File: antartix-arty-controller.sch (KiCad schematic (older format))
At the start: 113 parts, among them IC1 FT2232D, J1 QTE-020-04-L-D-A, J2 614004185023, J3 614004185023, J4 614004185023, J5 WE_629105150521, J6 0022232041, U1 PCT2075GVX, U2 PAC1934T-I_JQ, U3 USB2514B-I_M2, U4 TPS2024DR, U5 TPS2024DR, U6 TPS2024DR, Y1 7C-24.000MBB-T, Y2 MQ-6.000-12-30_30_

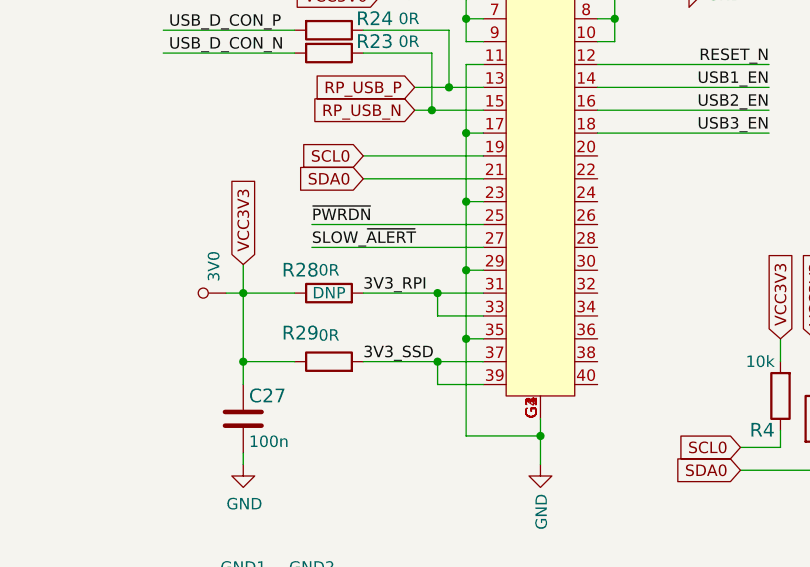
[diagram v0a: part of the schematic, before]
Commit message: Merge PCB design - Revision bumped to 1.1.0
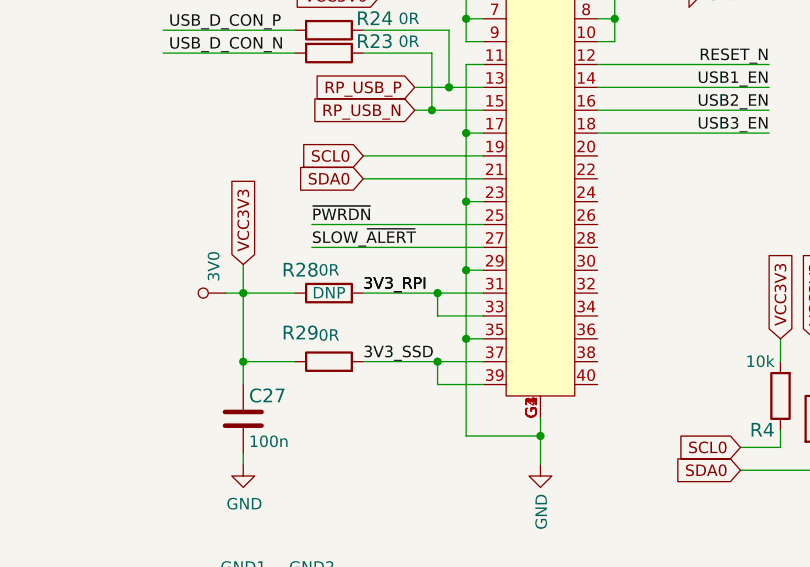
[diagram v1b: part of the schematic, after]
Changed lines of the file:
@@
 F1 "antartix-hdmi-adapter.sch" 50
 $EndSheet
+Text Label 1425 3225 0    50   ~ 0
+3V3_RPI
 $EndSCHEMATC

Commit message: Add hierarchical structure
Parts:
- removed 3V0, 5V0, GND1, GND2: TP_SMD1MM, antartix-arty-controller-footprints:Testpoint_smd_1mm, symbol antartix-arty-controller:TP_SMD1MM
- removed C1, C10, C11, C12, C13, C14, C15, C16, C17, C18, C2, C20, C22, C23, C24, C26, C27, C3, C32, C34, C35, C41, C42, C43, C44, C45, C46, C49, C5, C7, C9: C_100n_0402, antartix-arty-controller-footprints:0402-cap, symbol antartix-arty-controller:C_100n_0402
- removed C19, C21: C_22p_0402, antartix-arty-controller-footprints:0402-cap, symbol antartix-arty-controller:C_22p_0402
- removed C28, C29, C30: C_100n_0603, antmicro-footprints:0603-cap, symbol antmicroCapacitors0603:C_100n_0603
- removed C31, C33, C37, C47, C48: C_470u_KEMET_D, antartix-arty-controller-footprints:KEMET_D, symbol antartix-arty-controller:C_470u_KEMET_D
- removed C36, C38, C39: C_22u_0603, antmicro-footprints:0603-cap, symbol antmicroCapacitors0603:C_22u_0603
- removed C4, C6, C8: C_47p_0402, antartix-arty-controller-footprints:0402-cap, symbol antartix-arty-controller:C_47p_0402
- removed C40: C_1u_0402, antmicro-footprints:0402-cap, symbol antmicroCapacitors0402:C_1u_0402
- removed D1, D2, D3, D4, D5, D7: LG_L29K-G2J1-24-Z, antartix-arty-controller-footprints:LED_0603, symbol antartix-arty-controller:LG_L29K-G2J1-24-Z
- removed D6: TPD2E009, antartix-arty-controller-footprints:SOT-3, symbol antartix-arty-controller:TPD2E009
- removed FB1: BLM21SP111BH1, antartix-arty-controller-footprints:0805-res, symbol antartix-arty-controller:BLM21SP111BH1
- removed IC1: FT2232D, antartix-arty-controller-footprints:LQFP-48_7x7mm, symbol antartix-arty-controller:FT2232D
- removed J1: QTE-020-04-L-D-A, antartix-arty-controller-footprints:QTE-020-04-L-D-A, symbol antartix-arty-controller:QTE-020-04-L-D-A
- removed J2, J3, J4: 614004185023, 614004185023, symbol antmicroUSBDVIHDMIConnectors:614004185023
- removed J5: WE_629105150521, antartix-arty-controller-footprints:USB_Micro_B_Female_629105150521, symbol antartix-arty-controller:WE_629105150521
- removed J6: 0022232041, antmicro-footprints:PinHeader_1x4_P2.54mm_Drill1.02mm, symbol antartix-arty-controller:0022232041
- removed N1: antmicro_logo, antmicro-footprints:antmicro-logo_scaled_15mm, symbol antmicroMechanicalParts:antmicro_logo
- removed N2: oshw_logo, antmicro-footprints:oshw-logo, symbol antmicroMechanicalParts:oshw_logo
- removed R1, R30: R_47k_0402, antartix-arty-controller-footprints:0402-res, symbol antartix-arty-controller:R_47k_0402
- removed R10, R11, R12, R13, R17: R_470R_0402, antartix-arty-controller-footprints:0402-res, symbol antartix-arty-controller:R_470R_0402
- removed R14, R6, R7, R8: R_0R01_1206, antartix-arty-controller-footprints:1206-res, symbol antartix-arty-controller:R_0R01_1206
- removed R15, R33, R34, R35: R_4k7_0402, antartix-arty-controller-footprints:0402-res, symbol antartix-arty-controller:R_4k7_0402
- removed R16, R4, R5: R_10k_0402, antartix-arty-controller-footprints:0402-res, symbol antartix-arty-controller:R_10k_0402
- removed R18: R_1k54_0402, antartix-arty-controller-footprints:0402-res, symbol antartix-arty-controller:R_1k54_0402
- removed R19, R25, R36, R37: R_220R_0402, antartix-arty-controller-footprints:0402-res, symbol antartix-arty-controller:R_220R_0402
- removed R2, R3: R_100k_0402, antartix-arty-controller-footprints:0402-res, symbol antartix-arty-controller:R_100k_0402
- removed R20, R21, R22, R23, R24, R26, R27: R_0R_0402, antartix-arty-controller-footprints:0402-res, symbol antartix-arty-controller:R_0R_0402
- removed R28, R29: R_0R_0805, antmicro-footprints:0805-res, symbol antmicroResistorsmisc:R_0R_0805
- removed R31: R_12k_0402, antmicro-footprints:0402-res, symbol antmicroResistors0402:R_12k_0402
- removed R9: R_22R_0402, antartix-arty-controller-footprints:0402-res, symbol antartix-arty-controller:R_22R_0402
- removed U1: PCT2075GVX, antartix-arty-controller-footprints:SOT95P275X110-6N, symbol antartix-arty-controller:PCT2075GVX
- removed U2: PAC1934T-I_JQ, antartix-arty-controller-footprints:QFN65P400X400X55-17N, symbol antartix-arty-controller:PAC1934T-I_JQ
- removed U3: USB2514B-I_M2, antartix-arty-controller-footprints:QFN50P600X600X100-37N, symbol antartix-arty-controller:USB2514B-I_M2
- removed U4, U5, U6: TPS2024DR, antartix-arty-controller-footprints:SOIC-8_W3.9mm, symbol antartix-arty-controller:TPS2024DR
- removed Y1: 7C-24.000MBB-T, antartix-arty-controller-footprints:7C-24.000MBB-T, symbol antartix-arty-controller:7C-24.000MBB-T
- removed Y2: MQ-6.000-12-30_30_, antartix-arty-controller-footprints:Crystal_5x7mm, symbol antartix-arty-controller:MQ-6.000-12-30_30_
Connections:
- no-connect marks 4 -> 0
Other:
- note removed: "B2B connector"
- note removed: "Current monitor"
- note removed: "FTDI USB->I2C"
- note removed: "FTDI power filtering"
- note removed: "Hub power filtering"
- note removed: "LED indicators"
- note removed: "Micro USB connector"
- note removed: "Power switches"
- note removed: "Temperature sensor"
- note removed: "USB A connectors"
- note removed: "USB hub"
